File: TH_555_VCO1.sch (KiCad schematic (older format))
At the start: 28 parts

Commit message: 555
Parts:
- added C?: 100p, Capacitor_SMD:C_0805_2012Metric_Pad1.15x1.40mm_HandSolder, symbol Device:C
- added C? (x3): 1n, Capacitor_SMD:C_0805_2012Metric_Pad1.15x1.40mm_HandSolder, symbol Device:C
- added C?: 220n, Capacitor_SMD:C_0805_2012Metric_Pad1.15x1.40mm_HandSolder, symbol Device:C
- added D? (x2): 1N1007, Diode_SMD:D_SOD-123, symbol Device:D
- added Q? (x2): UMX1N, Package_TO_SOT_SMD:SOT-363_SC-70-6_Handsoldering, symbol UMX1N:UMX1N
- added Q?: MMBT2222A, SOT23, symbol MMBT2222A:MMBT2222A
- added R?: 1M, Resistor_SMD:R_0805_2012Metric_Pad1.15x1.40mm_HandSolder, symbol Device:R
- added R?: 2k4, Resistor_SMD:R_0805_2012Metric_Pad1.15x1.40mm_HandSolder, symbol Device:R
- added R?: 82R, Resistor_SMD:R_0805_2012Metric_Pad1.15x1.40mm_HandSolder, symbol Device:R
- added R?: 910R, Resistor_SMD:R_0805_2012Metric_Pad1.15x1.40mm_HandSolder, symbol Device:R
- added R?: 56k, Resistor_SMD:R_0805_2012Metric_Pad1.15x1.40mm_HandSolder, symbol Device:R
- added R? (x4): 47k, Resistor_SMD:R_0805_2012Metric_Pad1.15x1.40mm_HandSolder, symbol Device:R
- added R?: 10k, Resistor_SMD:R_0805_2012Metric_Pad1.15x1.40mm_HandSolder, symbol Device:R_Small
- added RV?: 100k FM, Potentiometer_THT:Potentiometer_China_RK09_Single_Vertical_AJ, symbol Device:R_POT
- added U? (x3): TL074, symbol Amplifier_Operational:TL074
- added U?: TLC555, AJ-Dropbox-Kicad:AJ_SO-8_5.3x6.2mm_P1.27mm, symbol Timer:TLC555
- R?: value 10k -> 47k
- RV?: value 100k CV2 -> 100k FM_exp
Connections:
- net labels added: 555_Dis, 555_In, 555_Out, GNDA, VCO_Control, VCO_Exp, b1, c1, e1
- net labels removed: 555_Out1
- wire segments 65 -> 126
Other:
- moved on the sheet: D?, R?, RV?

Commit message: 555 Core VCO Schematic
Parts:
- removed C?: 100p, Capacitor_SMD:C_0805_2012Metric_Pad1.15x1.40mm_HandSolder, symbol Device:C
- removed J?: FM_exp, AJ-Dropbox-Kicad:PJ301SM, symbol Connector:AudioJack2_SwitchT
- removed Q? (x2): UMX1N, Package_TO_SOT_SMD:SOT-363_SC-70-6_Handsoldering, symbol UMX1N:UMX1N
- removed R?: 910R, Resistor_SMD:R_0805_2012Metric_Pad1.15x1.40mm_HandSolder, symbol Device:R
- removed R?: 56k, Resistor_SMD:R_0805_2012Metric_Pad1.15x1.40mm_HandSolder, symbol Device:R
- removed R?: 47k, Resistor_SMD:R_0805_2012Metric_Pad1.15x1.40mm_HandSolder, symbol Device:R
- removed RV?: 100k FM_exp, Potentiometer_THT:Potentiometer_China_RK09_Single_Vertical_AJ, symbol Device:R_POT
- added C?: 10n, Capacitor_SMD:C_0805_2012Metric_Pad1.15x1.40mm_HandSolder, symbol Device:C
- added C?: 100n, Capacitor_SMD:C_0805_2012Metric_Pad1.15x1.40mm_HandSolder, symbol Device:C
- added C?: 22n, Capacitor_SMD:C_0805_2012Metric_Pad1.15x1.40mm_HandSolder, symbol Device:C
- added D?: Vactrol, symbol Device:LED
- added R? (x2): 62k, Resistor_SMD:R_0805_2012Metric_Pad1.15x1.40mm_HandSolder, symbol Device:R
- added R?: 100k_test, Resistor_SMD:R_0805_2012Metric_Pad1.15x1.40mm_HandSolder, symbol Device:R
- added R?: 1k5, Resistor_SMD:R_0805_2012Metric_Pad1.15x1.40mm_HandSolder, symbol Device:R
- added R?: LDR03, OptoDevice:R_LDR_10x8.5mm_P7.6mm_Vertical, symbol Sensor_Optical:LDR03
- added R? (x2): 47k, Resistor_SMD:R_0805_2012Metric_Pad1.15x1.40mm_HandSolder, symbol Device:R
- added R?: 100r, Resistor_SMD:R_0805_2012Metric_Pad1.15x1.40mm_HandSolder, symbol Device:R
- added R?: 12k, Resistor_SMD:R_0805_2012Metric_Pad1.15x1.40mm_HandSolder, symbol Device:R
- added R? (x2): 100k, Resistor_SMD:R_0805_2012Metric_Pad1.15x1.40mm_HandSolder, symbol Device:R
- added R?: 150k, Resistor_SMD:R_0805_2012Metric_Pad1.15x1.40mm_HandSolder, symbol Device:R
- added R?: 10k, Resistor_SMD:R_0805_2012Metric_Pad1.15x1.40mm_HandSolder, symbol Device:R
- added RV?: 5k, symbol Device:R_POT_TRIM
- added U? (x2): TL074, symbol Amplifier_Operational:TL074
- R?: value 1M -> 47k
- R?: value 2k4 -> 100k_test
- R?: value 82R -> 1k
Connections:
- net +12V: now also R?.1, R?.1, R?.2; no longer R?.1
- net -12V: now also R?.1, R?.2
- net 555_CV: now also J?.T, R?.1; no longer R?.2
- net 555_Dis: now also R?.1
- net 555_FM: now also R?.1, RV?.2; no longer R?.2
- net 555_In: now also R?.2, U?.8, U?.9 (-)
- net 555_Out: now also R?.2
- net GND: now also R?.2, C?.2, C?.2, D?.1 (K), R?.2, R?.2, U?.12 (+); no longer U?.3 (+), U?.5 (+)
- net VCO_Control: now also R?.2, R?.2, U?.3 (+); no longer R?.1, U?.2 (-)
- net at U?.7: now also R?.2
- net b1: no longer names the net of R?.1
- net b1: now also RV?.3
- net c1 renamed inv6
- net inv6: now also C?.2, R?.1, R?.2; no longer R?.2
- new net: R?.1, R?.1, U?.5 (+)
- new net: R?.1, R?.2, U?.2 (-)
- new net: D?.2 (A), RV?.1, RV?.2
- new net: R?.1, R?.1, R?.2
- new net: C?.1, R?.1, R?.2
- new net: C?.1, C?.1, R?.1, U?.10 (+)
- new net: R?.1, R?.2, U?.14
- new net inv13: R?.1, R?.1, R?.2, U?.13 (-)
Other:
- note added: "555 Core"
- note added: "555 Feedback filter"
- moved on the sheet: C?, D?, J?, Q?, R?, RV?, U?, U?A, U?B

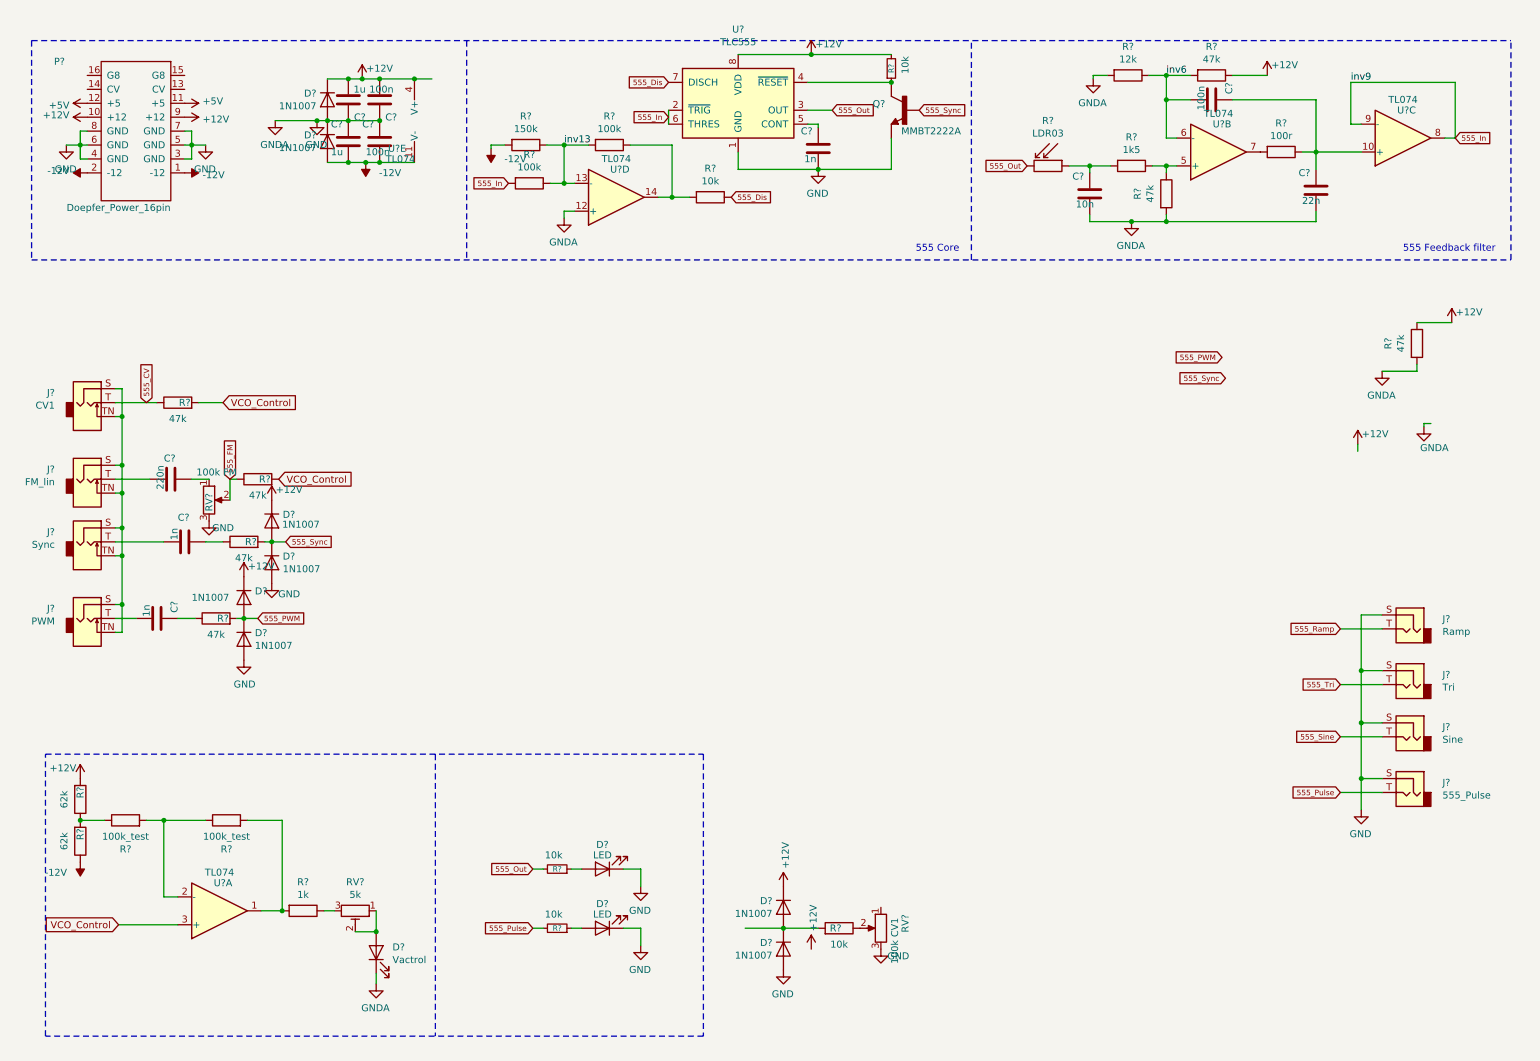
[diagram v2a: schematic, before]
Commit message: Sch for 555 VCO - Core - Sync - Tri - Ramp done
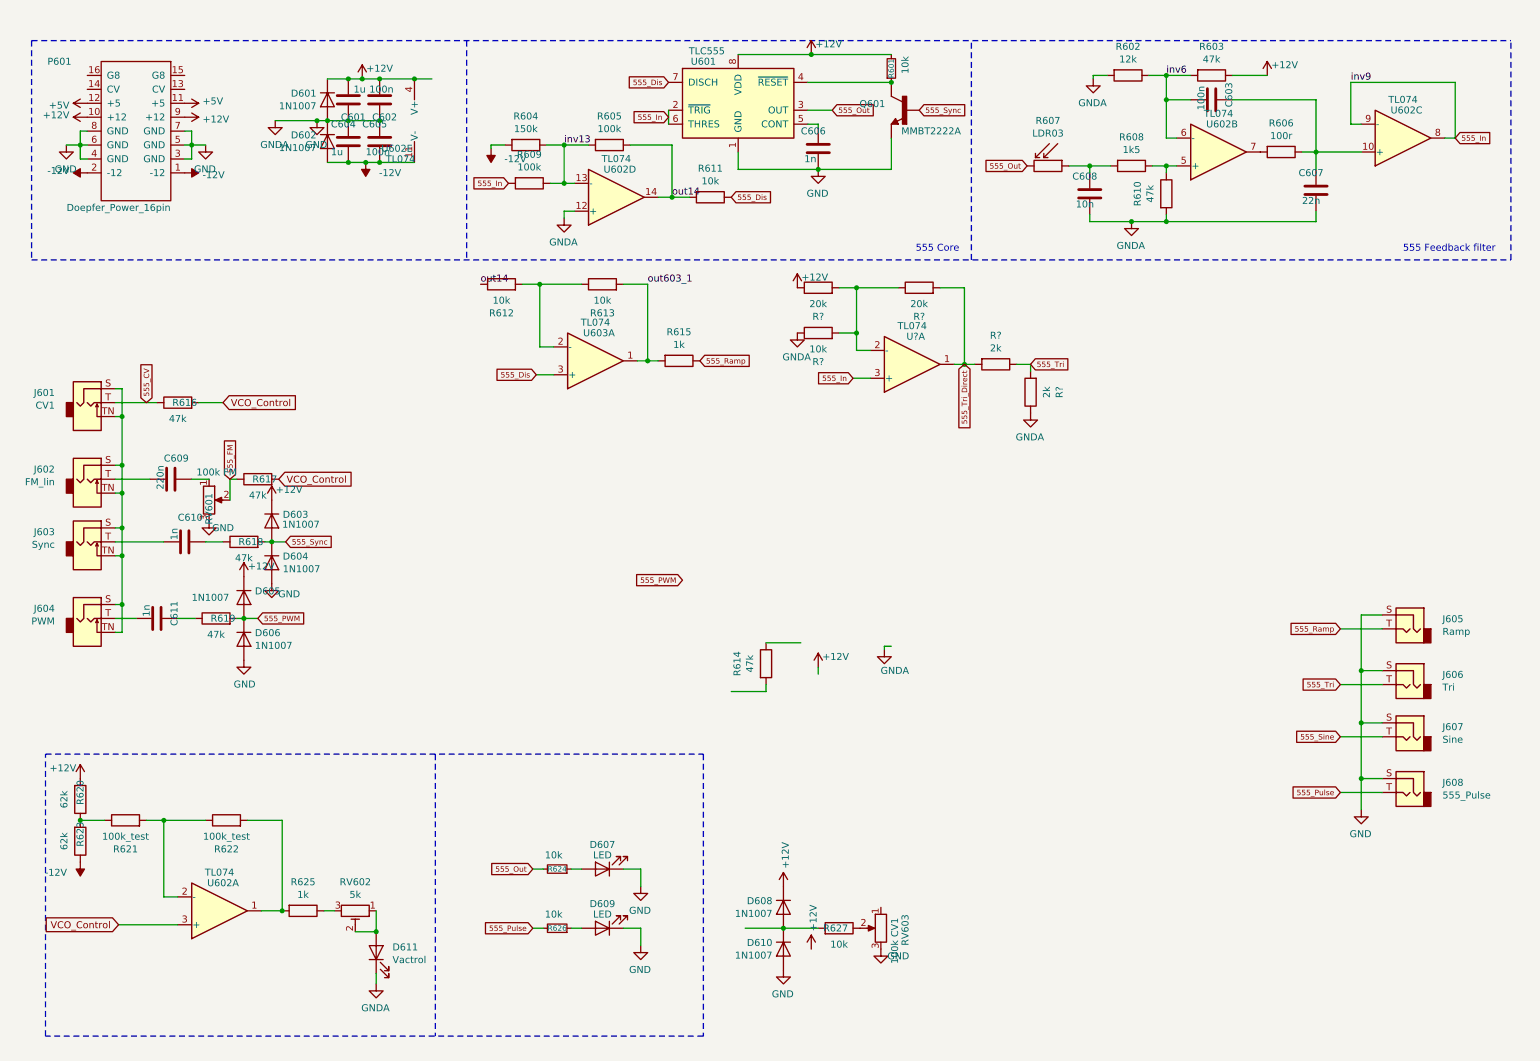
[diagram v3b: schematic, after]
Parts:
- added R612, R613, R?: 10k, Resistor_SMD:R_0805_2012Metric_Pad1.15x1.40mm_HandSolder, symbol Device:R
- added R615: 1k, Resistor_SMD:R_0805_2012Metric_Pad1.15x1.40mm_HandSolder, symbol Device:R
- added R? (x2): 20k, Resistor_SMD:R_0805_2012Metric_Pad1.15x1.40mm_HandSolder, symbol Device:R
- added R? (x2): 2k, Resistor_SMD:R_0805_2012Metric_Pad1.15x1.40mm_HandSolder, symbol Device:R
- added U603, U?: TL074, symbol Amplifier_Operational:TL074
- gave numbers to parts that had none: 61
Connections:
- net labels added: 555_Tri_Direct, out14, out603_1
- wire segments 150 -> 172
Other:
- moved on the sheet: R614

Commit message: 555 Tri Ramp Pulse
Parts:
- removed D608, D610: 1N1007, Diode_SMD:D_SOD-123, symbol Device:D
- removed R614: 47k, Resistor_SMD:R_0805_2012Metric_Pad1.15x1.40mm_HandSolder, symbol Device:R
- removed R627: 10k, Resistor_SMD:R_0805_2012Metric_Pad1.15x1.40mm_HandSolder, symbol Device:R
- added R? (x2): 100k, Resistor_SMD:R_0805_2012Metric_Pad1.15x1.40mm_HandSolder, symbol Device:R
- added R?: 150k, Resistor_SMD:R_0805_2012Metric_Pad1.15x1.40mm_HandSolder, symbol Device:R
- added R?: 2k2, Resistor_SMD:R_0805_2012Metric_Pad1.15x1.40mm_HandSolder, symbol Device:R
- added R?: 2M2, Resistor_SMD:R_0805_2012Metric_Pad1.15x1.40mm_HandSolder, symbol Device:R
- added R?: 3k, Resistor_SMD:R_0805_2012Metric_Pad1.15x1.40mm_HandSolder, symbol Device:R
- added R?: 1k8, Resistor_SMD:R_0805_2012Metric_Pad1.15x1.40mm_HandSolder, symbol Device:R
- added U? (x2): TL074, symbol Amplifier_Operational:TL074
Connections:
- wire segments 172 -> 187
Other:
- moved on the sheet: C609, C610, C611, D603, D604, D605, D606, J601, J602, J603, J604, J605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

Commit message: LDR
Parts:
- R607: footprint OptoDevice:R_LDR_10x8.5mm_P7.6mm_Vertical -> OptoDevice:R_LDR_4.9x4.2mm_P2.54mm_Vertical
- U603: renamed from U?; footprint (none) -> AJ-Dropbox-Kicad:AJ_SO-8_5.3x6.2mm_P1.27mm
- gave numbers to parts that had none: 13
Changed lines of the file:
@@
 F 0 "R607" V 7500 1425 50  0000 C CNN
 F 1 "LDR03" V 7591 1425 50  0000 C CNN
-F 2 "OptoDevice:R_LDR_10x8.5mm_P7.6mm_Vertical" V 8000 1425 50  0001 C CNN
+F 2 "OptoDevice:R_LDR_4.9x4.2mm_P2.54mm_Vertical" V 8000 1425 50  0001 C CNN
 F 3 "http://www.elektronica-componenten.nl/WebRoot/StoreNL/Shops/61422969/54F1/BA0C/C664/31B9/2173/C0A8/2AB9/2AEF/LDR03IMP.pdf" H 7825 1375 50  0001 C CNN
 	1    7825 1425
@@
 AR Path="/5CEBAECA/5E16C373" Ref="R?"  Part="1"
 AR Path="/5DD87D87/5DDB8911/5E16C373" Ref="R?"  Part="1"
-AR Path="/5DD87D87/5E16C373" Ref="R?"  Part="1"
-F 0 "R?" V 9643 3675 50  0000 C CNN
+AR Path="/5DD87D87/5E16C373" Ref="R627"  Part="1"
+F 0 "R627" V 9643 3675 50  0000 C CNN
 F 1 "20k" V 9734 3675 50  0000 C CNN
 F 2 "Resistor_SMD:R_0805_2012Metric_Pad1.15x1.40mm_HandSolder" V 9780 3675 50  0001 C CNN
@@
 P 9800 4225
 AR Path="/5DD87D87/5DDB8911/5E16C37D" Ref="U?"  Part="1"
-AR Path="/5DD87D87/5E16C37D" Ref="U?"  Part="2"
-F 0 "U?" H 9825 4025 50  0000 C CNN
+AR Path="/5DD87D87/5E16C37D" Ref="U603"  Part="2"
+F 0 "U603" H 9825 4025 50  0000 C CNN
 F 1 "TL074" H 9800 3949 50  0000 C CNN
-F 2 "" H 9750 4325 50  0001 C CNN
+F 2 "AJ-Dropbox-Kicad:AJ_SO-8_5.3x6.2mm_P1.27mm" H 9750 4325 50  0001 C CNN
 F 3 "http://www.ti.com/lit/ds/symlink/tl071.pdf" H 9850 4425 50  0001 C CNN
 	2    9800 4225
@@
 AR Path="/5CEBAECA/5E16C38A" Ref="R?"  Part="1"
 AR Path="/5DD87D87/5DDB8911/5E16C38A" Ref="R?"  Part="1"
-AR Path="/5DD87D87/5E16C38A" Ref="R?"  Part="1"
-F 0 "R?" V 10193 4225 50  0000 C CNN
+AR Path="/5DD87D87/5E16C38A" Ref="R629"  Part="1"
+F 0 "R629" V 10193 4225 50  0000 C CNN
 F 1 "2k" V 10284 4225 50  0000 C CNN
 F 2 "Resistor_SMD:R_0805_2012Metric_Pad1.15x1.40mm_HandSolder" V 10330 4225 50  0001 C CNN
@@
 AR Path="/5CEBAECA/5E16C394" Ref="R?"  Part="1"
 AR Path="/5DD87D87/5DDB8911/5E16C394" Ref="R?"  Part="1"
-AR Path="/5DD87D87/5E16C394" Ref="R?"  Part="1"
-F 0 "R?" V 8918 3675 50  0000 C CNN
+AR Path="/5DD87D87/5E16C394" Ref="R614"  Part="1"
+F 0 "R614" V 8918 3675 50  0000 C CNN
 F 1 "20k" V 9009 3675 50  0000 C CNN
 F 2 "Resistor_SMD:R_0805_2012Metric_Pad1.15x1.40mm_HandSolder" V 9055 3675 50  0001 C CNN
@@
 AR Path="/5CEBAECA/5E1810FC" Ref="R?"  Part="1"
 AR Path="/5DD87D87/5DDB8911/5E1810FC" Ref="R?"  Part="1"
-AR Path="/5DD87D87/5E1810FC" Ref="R?"  Part="1"
-F 0 "R?" V 8918 4000 50  0000 C CNN
+AR Path="/5DD87D87/5E1810FC" Ref="R628"  Part="1"
+F 0 "R628" V 8918 4000 50  0000 C CNN
 F 1 "10k" V 9009 4000 50  0000 C CNN
 F 2 "Resistor_SMD:R_0805_2012Metric_Pad1.15x1.40mm_HandSolder" V 9055 4000 50  0001 C CNN
@@
 AR Path="/5CEBAECA/5E18B2B4" Ref="R?"  Part="1"
 AR Path="/5DD87D87/5DDB8911/5E18B2B4" Ref="R?"  Part="1"
-AR Path="/5DD87D87/5E18B2B4" Ref="R?"  Part="1"
-F 0 "R?" V 10443 4425 50  0000 C CNN
+AR Path="/5DD87D87/5E18B2B4" Ref="R630"  Part="1"
+F 0 "R630" V 10443 4425 50  0000 C CNN
 F 1 "2k" V 10534 4425 50  0000 C CNN
 F 2 "Resistor_SMD:R_0805_2012Metric_Pad1.15x1.40mm_HandSolder" V 10580 4425 50  0001 C CNN
@@
 AR Path="/5CEBAECA/5E1946F7" Ref="#PWR?"  Part="1"
 AR Path="/5DD87D87/5DDB8911/5E1946F7" Ref="#PWR?"  Part="1"
-AR Path="/5DD87D87/5E1946F7" Ref="#PWR?"  Part="1"
-F 0 "#PWR?" H 10650 4325 50  0001 C CNN
+AR Path="/5DD87D87/5E1946F7" Ref="#PWR0622"  Part="1"
+F 0 "#PWR0622" H 10650 4325 50  0001 C CNN
 F 1 "GNDA" H 10655 4402 50  0000 C CNN
 F 2 "" H 10650 4575 50  0001 C CNN
@@
 P 8925 6000
 AR Path="/5DD87D87/5DDB8911/5E21E979" Ref="U?"  Part="2"
-AR Path="/5DD87D87/5E21E979" Ref="U?"  Part="4"
-F 0 "U?" H 8950 5800 50  0000 C CNN
+AR Path="/5DD87D87/5E21E979" Ref="U603"  Part="4"
+F 0 "U603" H 8950 5800 50  0000 C CNN
 F 1 "TL074" H 8925 5724 50  0000 C CNN
 F 2 "" H 8875 6100 50  0001 C CNN
@@
 AR Path="/5CEBAECA/5E21E983" Ref="R?"  Part="1"
 AR Path="/5DD87D87/5DDB8911/5E21E983" Ref="R?"  Part="1"
-AR Path="/5DD87D87/5E21E983" Ref="R?"  Part="1"
-F 0 "R?" V 7843 5900 50  0000 C CNN
+AR Path="/5DD87D87/5E21E983" Ref="R637"  Part="1"
+F 0 "R637" V 7843 5900 50  0000 C CNN
 F 1 "100k" V 7934 5900 50  0000 C CNN
 F 2 "Resistor_SMD:R_0805_2012Metric_Pad1.15x1.40mm_HandSolder" V 7980 5900 50  0001 C CNN
@@
 AR Path="/5CEBAECA/5E21E990" Ref="R?"  Part="1"
 AR Path="/5DD87D87/5DDB8911/5E21E990" Ref="R?"  Part="1"
-AR Path="/5DD87D87/5E21E990" Ref="R?"  Part="1"
-F 0 "R?" V 8668 5625 50  0000 C CNN
+AR Path="/5DD87D87/5E21E990" Ref="R635"  Part="1"
+F 0 "R635" V 8668 5625 50  0000 C CNN
 F 1 "100k" V 8759 5625 50  0000 C CNN
 F 2 "Resistor_SMD:R_0805_2012Metric_Pad1.15x1.40mm_HandSolder" V 8805 5625 50  0001 C CNN
@@
 AR Path="/5CEBAECA/5E21E99D" Ref="R?"  Part="1"
 AR Path="/5DD87D87/5DDB8911/5E21E99D" Ref="R?"  Part="1"
-AR Path="/5DD87D87/5E21E99D" Ref="R?"  Part="1"
-F 0 "R?" V 8068 5625 50  0000 C CNN
+AR Path="/5DD87D87/5E21E99D" Ref="R634"  Part="1"
+F 0 "R634" V 8068 5625 50  0000 C CNN
 F 1 "150k" V 8159 5625 50  0000 C CNN
 F 2 "Resistor_SMD:R_0805_2012Metric_Pad1.15x1.40mm_HandSolder" V 8205 5625 50  0001 C CNN
@@
 AR Path="/5CEBAECA/5E21E9A7" Ref="#PWR?"  Part="1"
 AR Path="/5DD87D87/5DDB8911/5E21E9A7" Ref="#PWR?"  Part="1"
-AR Path="/5DD87D87/5E21E9A7" Ref="#PWR?"  Part="1"
-F 0 "#PWR?" H 8550 5900 50  0001 C CNN
+AR Path="/5DD87D87/5E21E9A7" Ref="#PWR0635"  Part="1"
+F 0 "#PWR0635" H 8550 5900 50  0001 C CNN
 F 1 "GNDA" H 8555 5977 50  0000 C CNN
 F 2 "" H 8550 6150 50  0001 C CNN
@@
 AR Path="/5CD3F059/5E21E9B4" Ref="#PWR?"  Part="1"
 AR Path="/5CE53731/5E21E9B4" Ref="#PWR?"  Part="1"
-AR Path="/5DD87D87/5E21E9B4" Ref="#PWR?"  Part="1"
-F 0 "#PWR?" H 8025 5750 50  0001 C CNN
+AR Path="/5DD87D87/5E21E9B4" Ref="#PWR0623"  Part="1"
+F 0 "#PWR0623" H 8025 5750 50  0001 C CNN
 F 1 "-12V" H 7850 5725 50  0000 C CNN
 F 2 "" H 8025 5650 50  0001 C CNN
@@
 P 9625 5525
 AR Path="/5DD87D87/5DDB8911/5E28854A" Ref="U?"  Part="2"
-AR Path="/5DD87D87/5E28854A" Ref="U?"  Part="3"
-F 0 "U?" H 9650 5325 50  0000 C CNN
+AR Path="/5DD87D87/5E28854A" Ref="U603"  Part="3"
+F 0 "U603" H 9650 5325 50  0000 C CNN
 F 1 "TL074" H 9625 5249 50  0000 C CNN
 F 2 "" H 9575 5625 50  0001 C CNN
@@
 AR Path="/5CEBAECA/5E28A4DD" Ref="R?"  Part="1"
 AR Path="/5DD87D87/5DDB8911/5E28A4DD" Ref="R?"  Part="1"
-AR Path="/5DD87D87/5E28A4DD" Ref="R?"  Part="1"
-F 0 "R?" V 8943 5100 50  0000 C CNN
+AR Path="/5DD87D87/5E28A4DD" Ref="R631"  Part="1"
+F 0 "R631" V 8943 5100 50  0000 C CNN
 F 1 "2k2" V 9034 5100 50  0000 C CNN
 F 2 "Resistor_SMD:R_0805_2012Metric_Pad1.15x1.40mm_HandSolder" V 9080 5100 50  0001 C CNN
@@
 AR Path="/5CEBAECA/5E28A81B" Ref="R?"  Part="1"
 AR Path="/5DD87D87/5DDB8911/5E28A81B" Ref="R?"  Part="1"
-AR Path="/5DD87D87/5E28A81B" Ref="R?"  Part="1"
-F 0 "R?" V 9443 5100 50  0000 C CNN
+AR Path="/5DD87D87/5E28A81B" Ref="R632"  Part="1"
+F 0 "R632" V 9443 5100 50  0000 C CNN
 F 1 "2M2" V 9534 5100 50  0000 C CNN
 F 2 "Resistor_SMD:R_0805_2012Metric_Pad1.15x1.40mm_HandSolder" V 9580 5100 50  0001 C CNN
@@
 AR Path="/5CEBAECA/5E2BE889" Ref="R?"  Part="1"
 AR Path="/5DD87D87/5DDB8911/5E2BE889" Ref="R?"  Part="1"
-AR Path="/5DD87D87/5E2BE889" Ref="R?"  Part="1"
-F 0 "R?" V 9968 5525 50  0000 C CNN
+AR Path="/5DD87D87/5E2BE889" Ref="R633"  Part="1"
+F 0 "R633" V 9968 5525 50  0000 C CNN
 F 1 "3k" V 10059 5525 50  0000 C CNN
 F 2 "Resistor_SMD:R_0805_2012Metric_Pad1.15x1.40mm_HandSolder" V 10105 5525 50  0001 C CNN
@@
 AR Path="/5CEBAECA/5E2BEDAF" Ref="R?"  Part="1"
 AR Path="/5DD87D87/5DDB8911/5E2BEDAF" Ref="R?"  Part="1"
-AR Path="/5DD87D87/5E2BEDAF" Ref="R?"  Part="1"
-F 0 "R?" V 10318 5750 50  0000 C CNN
+AR Path="/5DD87D87/5E2BEDAF" Ref="R636"  Part="1"
+F 0 "R636" V 10318 5750 50  0000 C CNN
 F 1 "1k8" V 10409 5750 50  0000 C CNN
 F 2 "Resistor_SMD:R_0805_2012Metric_Pad1.15x1.40mm_HandSolder" V 10455 5750 50  0001 C CNN
@@
 AR Path="/5CEBAECA/5E2BF23C" Ref="#PWR?"  Part="1"
 AR Path="/5DD87D87/5DDB8911/5E2BF23C" Ref="#PWR?"  Part="1"
-AR Path="/5DD87D87/5E2BF23C" Ref="#PWR?"  Part="1"
-F 0 "#PWR?" H 10525 5650 50  0001 C CNN
+AR Path="/5DD87D87/5E2BF23C" Ref="#PWR0633"  Part="1"
+F 0 "#PWR0633" H 10525 5650 50  0001 C CNN
 F 1 "GNDA" H 10530 5727 50  0000 C CNN
 F 2 "" H 10525 5900 50  0001 C CNN

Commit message: Before Sine PCB on 555
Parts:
- U602, U603: footprint (none) -> Package_SO:SOIC-14_3.9x8.7mm_P1.27mm
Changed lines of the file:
@@
 F 0 "U602" H 9075 1125 50  0000 C CNN
 F 1 "TL074" H 9050 1049 50  0000 C CNN
-F 2 "" H 9000 1425 50  0001 C CNN
+F 2 "Package_SO:SOIC-14_3.9x8.7mm_P1.27mm" H 9000 1425 50  0001 C CNN
 F 3 "http://www.ti.com/lit/ds/symlink/tl071.pdf" H 9100 1525 50  0001 C CNN
 	2    9050 1325
@@
 F 0 "U603" H 9875 2875 50  0000 C CNN
 F 1 "TL074" H 9850 2799 50  0000 C CNN
-F 2 "" H 9800 3175 50  0001 C CNN
+F 2 "Package_SO:SOIC-14_3.9x8.7mm_P1.27mm" H 9800 3175 50  0001 C CNN
 F 3 "http://www.ti.com/lit/ds/symlink/tl071.pdf" H 9900 3275 50  0001 C CNN
 	1    9850 3075
